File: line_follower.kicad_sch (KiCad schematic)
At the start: 93 parts, among them J1 Conn_01x20_Socket, J10 Conn_01x20_Pin, J11 Conn_01x20_Pin, J12 Conn_01x02_Socket, J2 Conn_01x20_Socket, J3 Conn_01x06_Socket, J4 Conn_01x06_Socket, J5 XT60-M, J6 Conn_01x02_Socket, J7 Conn_01x02_Socket, J8 Conn_01x06_Socket, J9 Conn_01x02_Socket, SW1 SW_Push, SW3 SW_Push, SW4 SW_Push, SW5 SW_Push

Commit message: placement done
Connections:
- net CALIB: now also R32.1; no longer D14.2 (A)
- net GND: now also D10.1 (K), D11.1 (K), D12.1 (K), D13.1 (K), D14.1 (K), D2.1 (K), D3.1 (K), D4.1 (K), D5.1 (K), D6.1 (K), D7.1 (K), D8.1 (K), D9.1 (K); no longer R20.2, R21.2, R22.2, R23.2, R24.2, R25.2, R26.2, R27.2, R28.2, R29.2, R30.2, R31.2, R32.2
- net IN1: now also J4.1 (Pin_1); no longer J4.6 (Pin_6)
- net IN2: now also J4.2 (Pin_2); no longer J4.5 (Pin_5)
- net IN3: now also J4.5 (Pin_5); no longer J4.2 (Pin_2)
- net IN4: now also J4.6 (Pin_6); no longer J4.1 (Pin_1)
- net LEFT: now also R30.1; no longer D12.2 (A)
- net PA12: now also R23.2; no longer D5.2 (A)
- net PA15: now also R24.2; no longer D6.2 (A)
- net PB10: now also R27.2; no longer D9.2 (A)
- net PB12: now also R20.2; no longer D2.2 (A)
- net PB13: now also R21.2; no longer D3.2 (A)
- net PB14: now also R22.2; no longer D4.2 (A)
- net PB2: now also R28.2; no longer D10.2 (A)
- net PB3: now also R25.2; no longer D7.2 (A)
- net PB4: now also R26.2; no longer D8.2 (A)
- net PB9: now also R29.1; no longer D11.2 (A)
- net PC13: now also R31.1; no longer D13.2 (A)
- net at R21.1: now also D3.2 (A); no longer D3.1 (K)
- net at R23.1: now also D5.2 (A); no longer D5.1 (K)
- net at R27.1: now also D9.2 (A); no longer D9.1 (K)
- net at R22.1: now also D4.2 (A); no longer D4.1 (K)
- net at R26.1: now also D8.2 (A); no longer D8.1 (K)
- net at R28.1: now also D10.2 (A); no longer D10.1 (K)
- net at R24.1: now also D6.2 (A); no longer D6.1 (K)
- net at R25.1: now also D7.2 (A); no longer D7.1 (K)
- net at R20.1: now also D2.2 (A); no longer D2.1 (K)
- new net: D11.2 (A), R29.2
- new net: D12.2 (A), R30.2
- new net: D13.2 (A), R31.2
- new net: D14.2 (A), R32.2
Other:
- moved on the sheet: D10, D11, D12, D13, D14, D2, D3, D4, D5, D6, D7, D8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

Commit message: minor design errors left
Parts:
- added C22, C23: 22uf, Capacitor_SMD:C_0603_1608Metric_Pad1.08x0.95mm_HandSolder, symbol Device:C
- added J13: Conn_01x04_Pin, Connector_PinHeader_2.54mm:PinHeader_1x04_P2.54mm_Vertical, symbol Connector:Conn_01x04_Pin
- added U1: AMS1117-3.3, Package_TO_SOT_SMD:SOT-223-3_TabPin2, symbol Regulator_Linear:AMS1117-3.3
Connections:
- net 3.3V_STM: now also C23.1, U1.2 (VO); no longer C10.1, C11.1, C12.1, C3.1, C5.1, C6.1, C7.1, C8.1, C9.1
- net 5V_STM: now also C22.1, U1.3 (VI)
- net GND: now also C22.2, C23.2, U1.1 (GND)
- net LEFT: now also J1.19 (Pin_19), J11.19 (Pin_19); no longer J1.18 (Pin_18), J11.18 (Pin_18)
- net OUT1: now also J13.1 (Pin_1); no longer J3.3 (Pin_3), J3.4 (Pin_4), J3.5 (Pin_5)
- net PB9: now also SW5.2; no longer R29.1
- net PC15: now also R31.1; no longer SW5.2
- net RPR_ANO: now reaches A2.1, R3.2
- net RPR_ANO: now also A1.1, A3.1, A4.1, A5.1, A6.1, A7.1, A8.1, A9.1, C10.1, C11.1, C12.1, C3.1, C5.1, C6.1, C7.1, C8.1, C9.1, R10.2, R2.2, R4.2, R5.2, R6.2, R7.2, R8.2, R9.2
- removed net PC13: J1.19 (Pin_19), J11.19 (Pin_19), R31.1
- new net OUT2: J13.2 (Pin_2), J3.3 (Pin_3)
- new net OUT3: J13.3 (Pin_3), J3.4 (Pin_4)
- new net OUT4: J13.4 (Pin_4), J3.5 (Pin_5)
- new net PC14: J1.18 (Pin_18), J11.18 (Pin_18), R29.1
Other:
- note added: "SUPPLY FOR RPR220"
- moved on the sheet: D1, R1, SW1, SW4

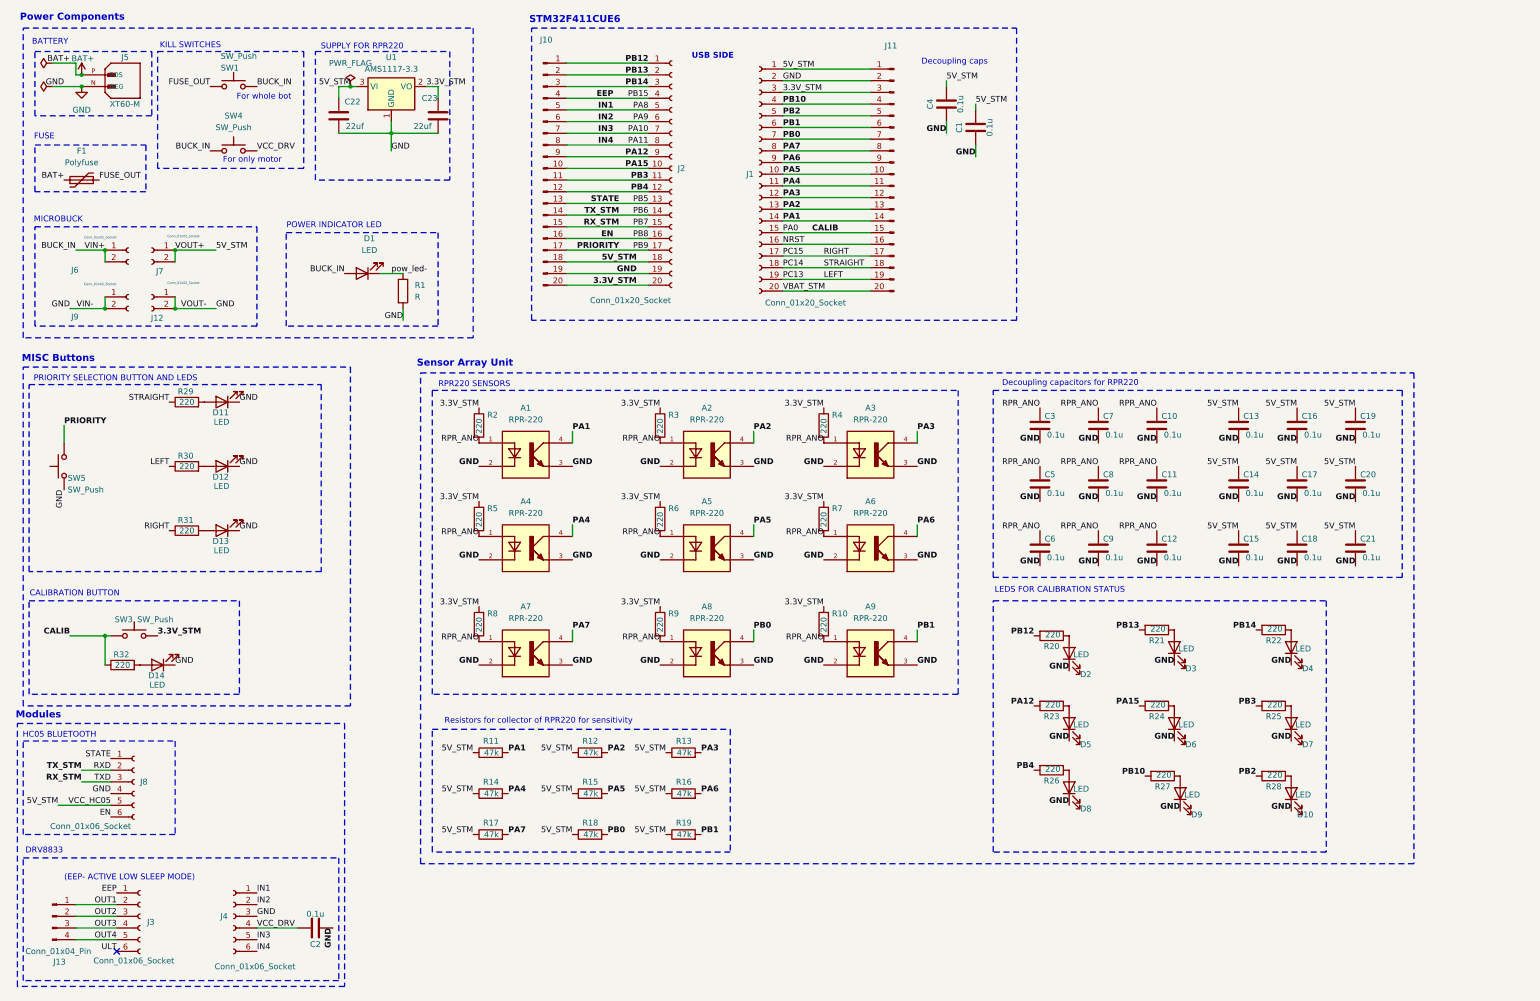
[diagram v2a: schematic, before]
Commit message: changed to emitter resistor
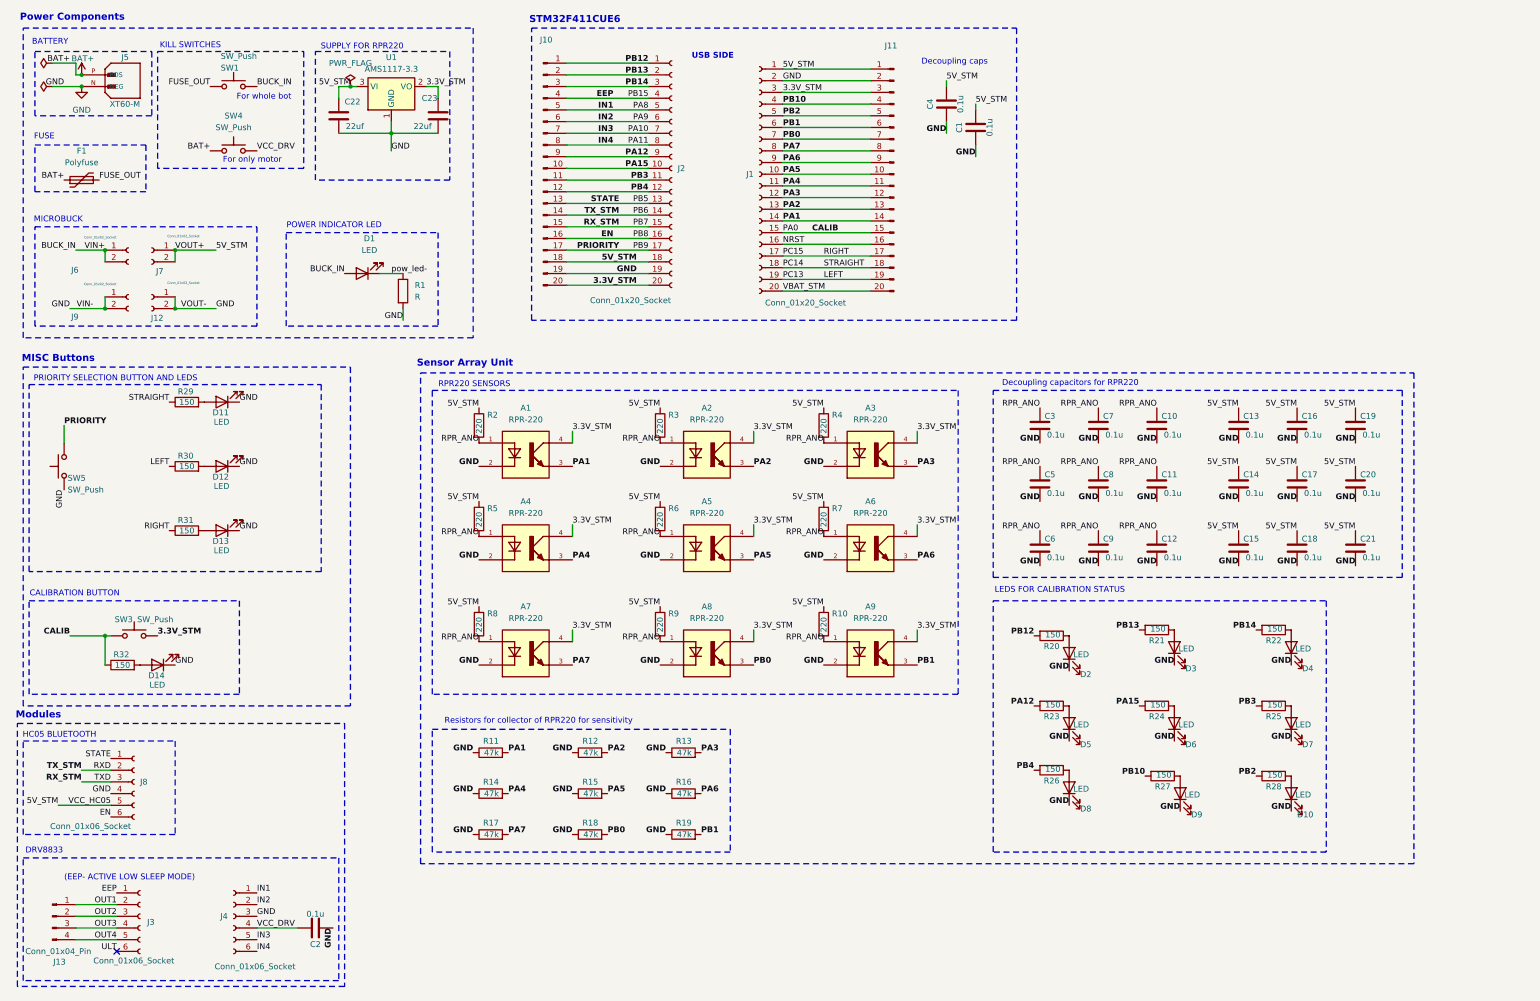
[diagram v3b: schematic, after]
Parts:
- R20, R21, R22, R23, R24, R25, R26, R27, R28, R29, R30, R31, R32: value 220 -> 150
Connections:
- net 3.3V_STM: now also A1.4, A2.4, A3.4, A4.4, A5.4, A6.4, A7.4, A8.4, A9.4; no longer R10.1, R2.1, R3.1, R4.1, R5.1, R6.1, R7.1, R8.1, R9.1
- net 5V_STM: now also R10.1, R2.1, R3.1, R4.1, R5.1, R6.1, R7.1, R8.1, R9.1; no longer R11.1, R12.1, R13.1, R14.1, R15.1, R16.1, R17.1, R18.1, R19.1
- net BAT+: now also SW4.1
- net BUCK_IN: no longer SW4.1
- net GND: now also R11.1, R12.1, R13.1, R14.1, R15.1, R16.1, R17.1, R18.1, R19.1; no longer A1.3, A2.3, A3.3, A4.3, A5.3, A6.3, A7.3, A8.3, A9.3
- net PA1: now also A1.3; no longer A1.4
- net PA2: now also A2.3; no longer A2.4
- net PA3: now also A3.3; no longer A3.4
- net PA4: now also A4.3; no longer A4.4
- net PA5: now also A5.3; no longer A5.4
- net PA6: now also A6.3; no longer A6.4
- net PA7: now also A7.3; no longer A7.4
- net PB0: now also A8.3; no longer A8.4
- net PB1: now also A9.3; no longer A9.4

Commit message: pcb finished
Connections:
- net 3.3V_STM: now also C13.1, C14.1, C15.1, C16.1, C17.1, C18.1, C19.1, C20.1, C21.1
- net 5V_STM: no longer C13.1, C14.1, C15.1, C16.1, C17.1, C18.1, C19.1, C20.1, C21.1
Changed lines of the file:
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@@
+		)
+	)
+	(label "3.3V_STM"
+		(at 287.02 130.81 180)
+		(effects
+			(font
+				(size 1.27 1.27)
+			)
+			(justify right bottom)
 		)
 	)
@@
 		)
 	)
-	(label "5V_STM"
+	(label "3.3V_STM"
 		(at 287.02 104.14 180)
 		(effects
@@
 		)
 	)
-	(label "5V_STM"
-		(at 312.42 116.84 180)
-		(effects
-			(font
-				(size 1.27 1.27)
-			)
-			(justify right bottom)
-		)
-	)
 	(label "PA6"
 		(at 217.17 137.16 0)
@@
 		)
 	)
+	(label "3.3V_STM"
+		(at 312.42 116.84 180)
+		(effects
+			(font
+				(size 1.27 1.27)
+			)
+			(justify right bottom)
+		)
+	)
 	(label "PB2"
 		(at 290.83 184.15 180)
@@
 	)
 	(label "3.3V_STM"
+		(at 299.72 116.84 180)
+		(effects
+			(font
+				(size 1.27 1.27)
+			)
+			(justify right bottom)
+		)
+	)
+	(label "3.3V_STM"
 		(at 181.61 129.54 0)
 		(effects
@@
 		)
 	)
-	(label "5V_STM"
-		(at 299.72 130.81 180)
-		(effects
-			(font
-				(size 1.27 1.27)
-			)
-			(justify right bottom)
-		)
-	)
 	(label "VCC_DRV"
 		(at 73.66 217.17 0)
@@
 		)
 	)
+	(label "3.3V_STM"
+		(at 312.42 130.81 180)
+		(effects
+			(font
+				(size 1.27 1.27)
+			)
+			(justify right bottom)
+		)
+	)
 	(label "PA3"
 		(at 187.96 58.42 0)
@@
 		)
 	)
-	(label "5V_STM"
-		(at 287.02 116.84 180)
-		(effects
-			(font
-				(size 1.27 1.27)
-			)
-			(justify right bottom)
-		)
-	)
 	(label "RPR_ANO"
 		(at 196.85 111.76 180)
@@
 		)
 	)
+	(label "3.3V_STM"
+		(at 299.72 130.81 180)
+		(effects
+			(font
+				(size 1.27 1.27)
+			)
+			(justify right bottom)
+		)
+	)
 	(label "PA11"
 		(at 158.75 46.99 180)
@@
 		)
 	)
+	(label "3.3V_STM"
+		(at 299.72 104.14 180)
+		(effects
+			(font
+				(size 1.27 1.27)
+			)
+			(justify right bottom)
+		)
+	)
+	(label "3.3V_STM"
+		(at 312.42 104.14 180)
+		(effects
+			(font
+				(size 1.27 1.27)
+			)
+			(justify right bottom)
+		)
+	)
 	(label "IN1"
 		(at 73.66 209.55 0)
@@
 		)
 	)
-	(label "5V_STM"
-		(at 312.42 130.81 180)
-		(effects
-			(font
-				(size 1.27 1.27)
-			)
-			(justify right bottom)
-		)
-	)
 	(label "VOUT+"
 		(at 55.88 69.85 0)
@@
 		)
 	)
-	(label "5V_STM"
-		(at 299.72 116.84 180)
-		(effects
-			(font
-				(size 1.27 1.27)
-			)
-			(justify right bottom)
-		)
-	)
 	(label "PA2"
 		(at 149.86 179.07 0)
@@
 		)
 	)
+	(label "3.3V_STM"
+		(at 287.02 116.84 180)
+		(effects
+			(font
+				(size 1.27 1.27)
+			)
+			(justify right bottom)
+		)
+	)
 	(label "PC15"
 		(at 187.96 71.12 0)
@@
 	)
 	(label "5V_STM"
-		(at 312.42 104.14 180)
-		(effects
-			(font
-				(size 1.27 1.27)
-			)
-			(justify right bottom)
-		)
-	)
-	(label "5V_STM"
 		(at 121.92 147.32 180)
 		(effects
@@
 		)
 	)
-	(label "5V_STM"
-		(at 299.72 104.14 180)
-		(effects
-			(font
-				(size 1.27 1.27)
-			)
-			(justify right bottom)
-		)
-	)
 	(label "pow_led-"
 		(at 102.87 74.93 0)
@@
 			)
 			(justify right bottom)
-		)
-	)
-	(label "5V_STM"
-		(at 287.02 130.81 180)
-		(effects
-			(font
-				(size 1.27 1.27)
-			)
-			(justify right bottom)

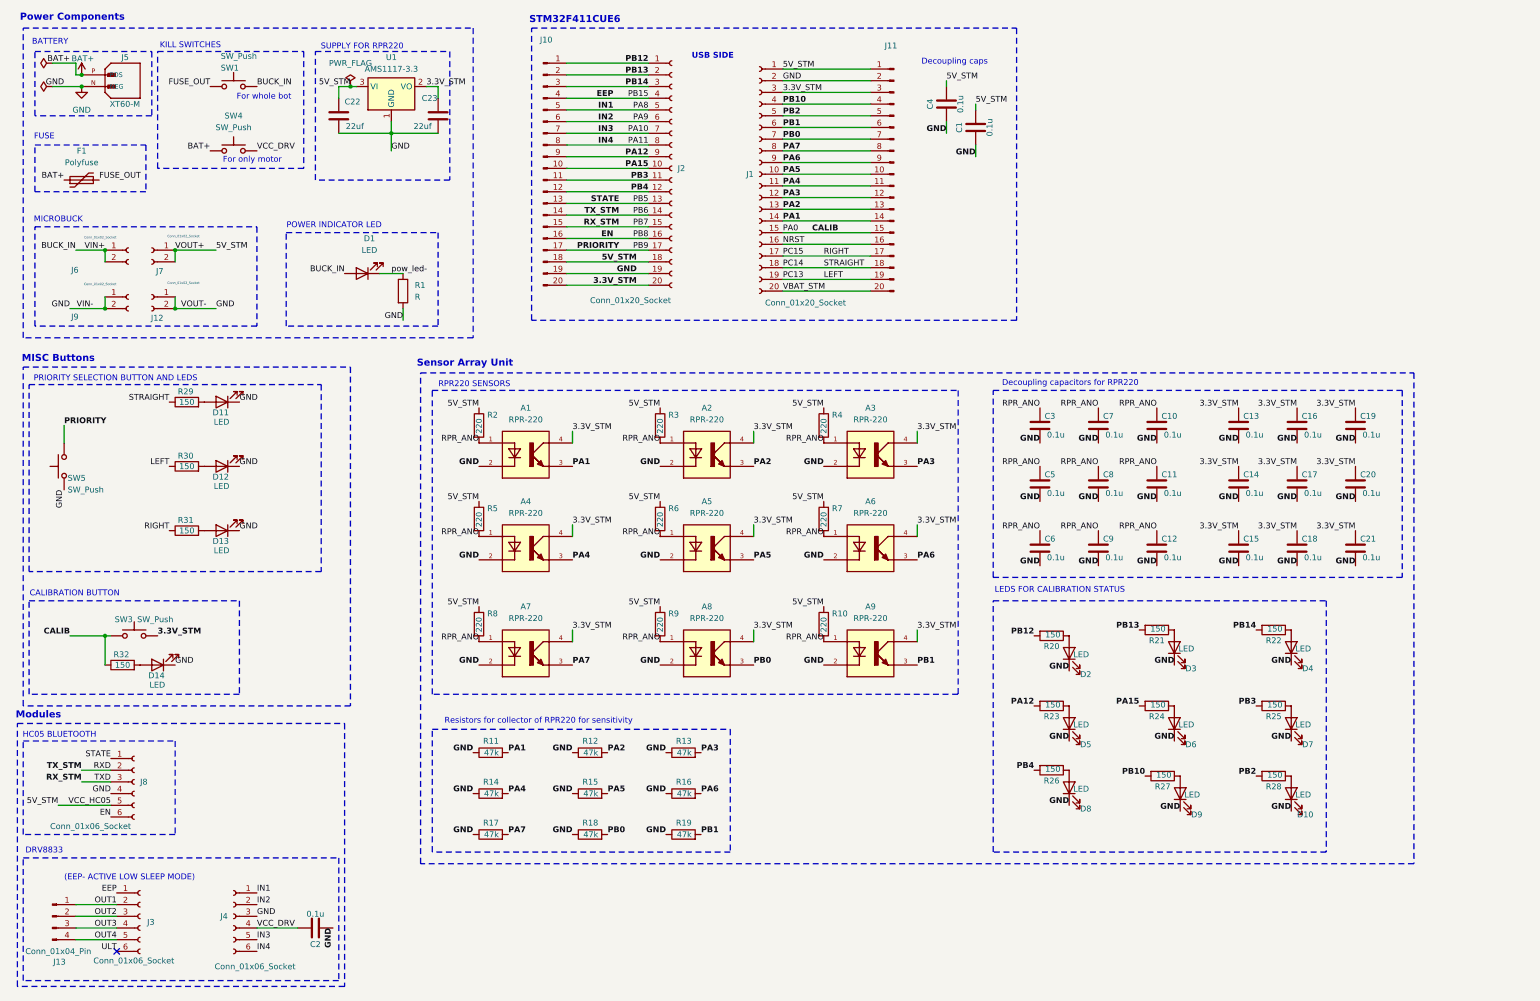
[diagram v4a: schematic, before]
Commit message: all drc errors fixed
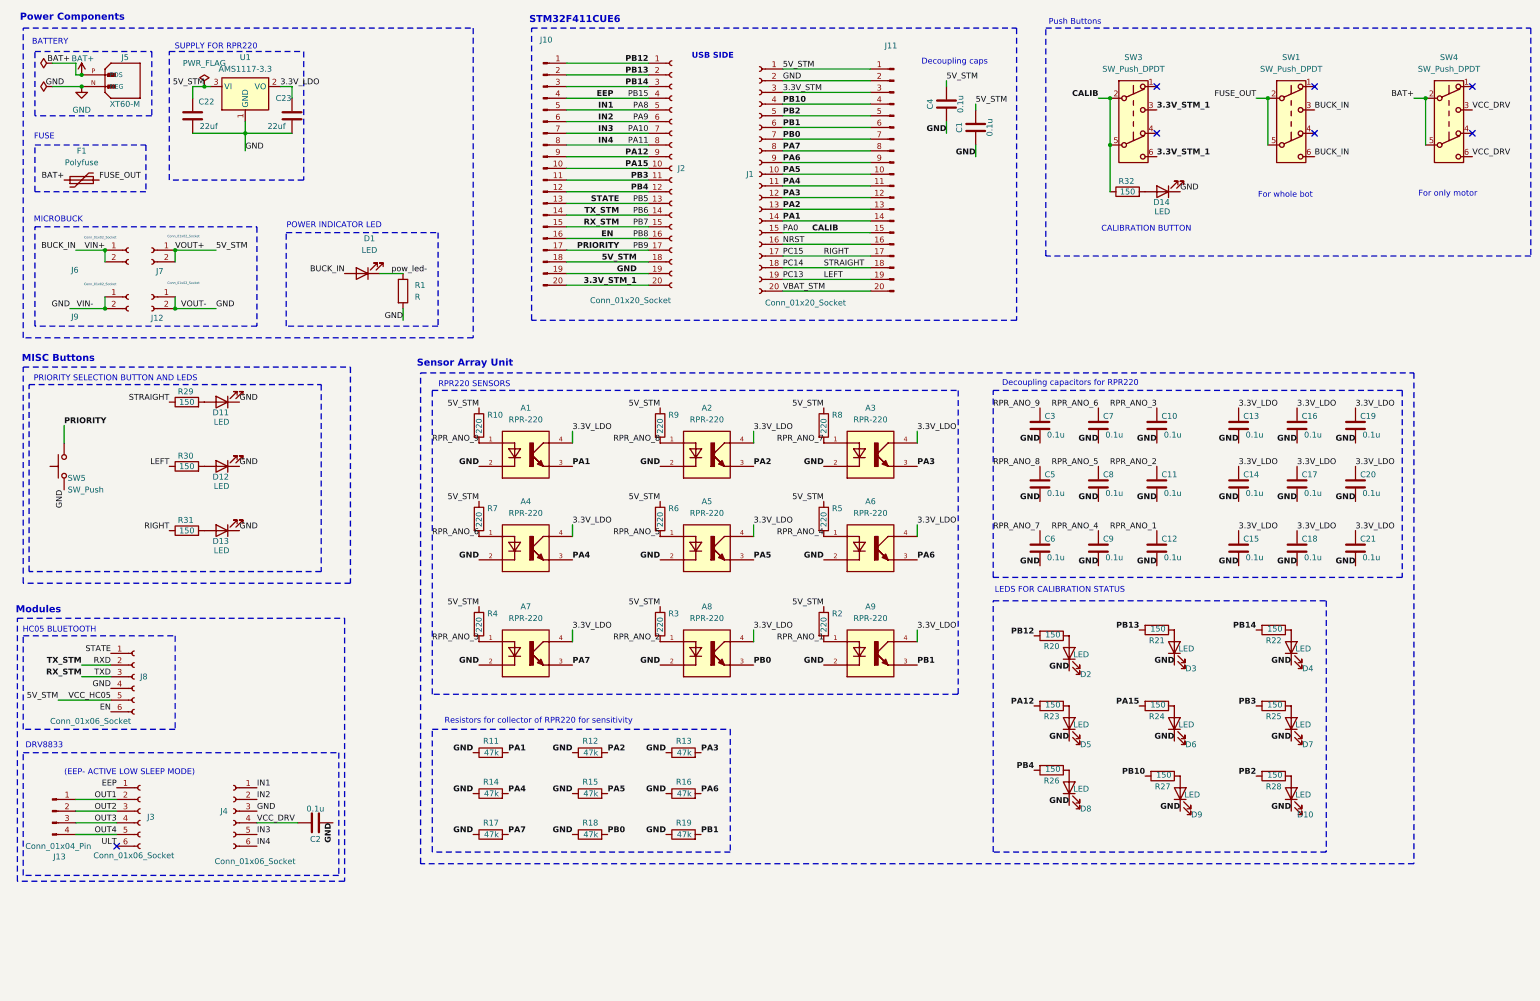
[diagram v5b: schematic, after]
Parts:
- removed SW1, SW3, SW4: SW_Push, Button_Switch_THT:SW_Push_2P2T_Toggle_CK_PVA2xxH3xxxxxxV2, symbol Switch:SW_Push
- added SW1, SW3, SW4: SW_Push_DPDT, Button_Switch_THT:SW_Push_2P2T_Toggle_CK_PVA2xxH3xxxxxxV2, symbol Switch:SW_Push_DPDT
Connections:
- net 3.3V_STM: no longer A1.4, A2.4, A3.4, A4.4, A5.4, A6.4, A7.4, A8.4, A9.4, C13.1, C14.1, C15.1, C16.1, C17.1, C18.1, C19.1, C20.1, C21.1, C23.1, J10.20 (Pin_20), J2.20 (Pin_20), U1.2 (VO)
- net BAT+: now also SW4.2 (B), SW4.5 (B)
- net BUCK_IN: now also SW1.3 (C), SW1.6 (C)
- net CALIB: now also SW3.2 (B), SW3.5 (B)
- net FUSE_OUT : now also SW1.2 (B), SW1.5 (B)
- net VCC_DRV: now also SW4.3 (C), SW4.6 (C)
- removed net RPR_ANO: A1.1, A2.1, A3.1, A4.1, A5.1, A6.1, A7.1, A8.1, A9.1, C10.1, C11.1, C12.1, C3.1, C5.1, C6.1, C7.1, C8.1, C9.1, R10.2, R2.2, R3.2, R4.2, R5.2, R6.2, R7.2, R8.2, R9.2
- new net 3.3V_LDO: A1.4, A2.4, A3.4, A4.4, A5.4, A6.4, A7.4, A8.4, A9.4, C13.1, C14.1, C15.1, C16.1, C17.1, C18.1, C19.1, C20.1, C21.1, C23.1, U1.2 (VO)
- new net 3.3V_STM_1: J10.20 (Pin_20), J2.20 (Pin_20), SW3.3 (C), SW3.6 (C)
- new net RPR_ANO_1: A9.1, C12.1, R2.2
- new net RPR_ANO_2: A8.1, C11.1, R3.2
- new net RPR_ANO_3: A7.1, C10.1, R4.2
- new net RPR_ANO_4: A6.1, C9.1, R5.2
- new net RPR_ANO_5: A5.1, C8.1, R6.2
- new net RPR_ANO_6: A4.1, C7.1, R7.2
- new net RPR_ANO_7: A3.1, C6.1, R8.2
- new net RPR_ANO_8: A2.1, C5.1, R9.2
- new net RPR_ANO_9: A1.1, C3.1, R10.2
- no-connect marks 1 -> 7
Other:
- note added: "Push Buttons"
- note removed: "KILL SWITCHES"
- moved on the sheet: C2, C22, C23, D14, J13, J3, J4, J8, R10, R2, R3, R32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
